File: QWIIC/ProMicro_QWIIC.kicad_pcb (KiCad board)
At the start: 2 copper layers, 17.8 x 30.5 mm, 19 parts, among them J1 Qwiic, J2 Qwiic, J3 Conn_01x02, J4 Conn_01x02, J5 Conn_01x03, J6 Conn_01x03, U1 ADS1015IDGS, U2 BME280

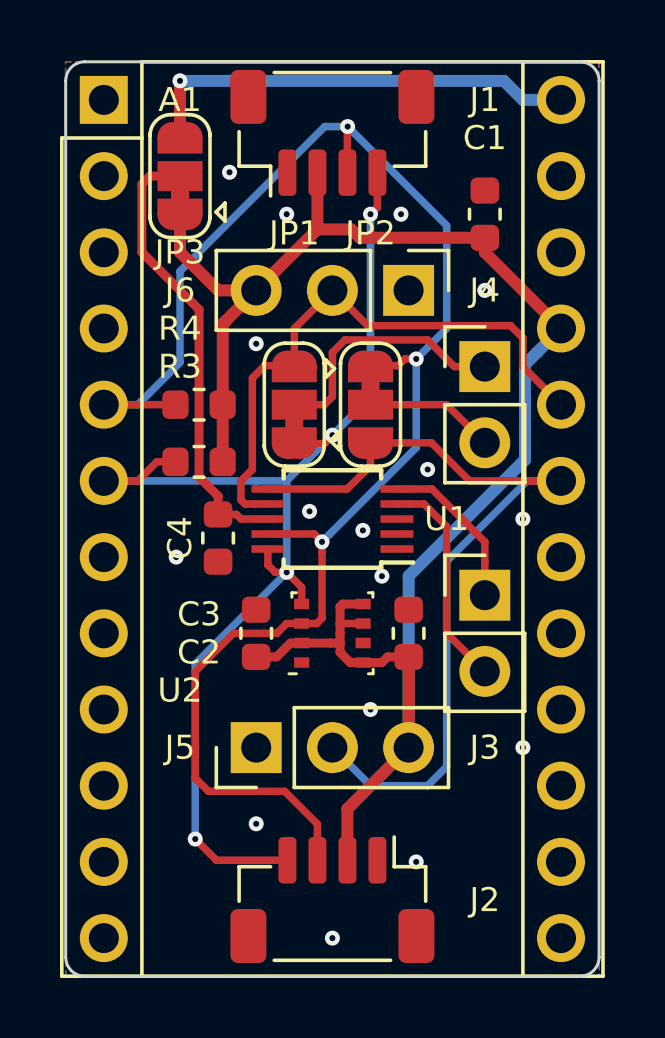
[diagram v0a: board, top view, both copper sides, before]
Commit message: make controller holes wide enough
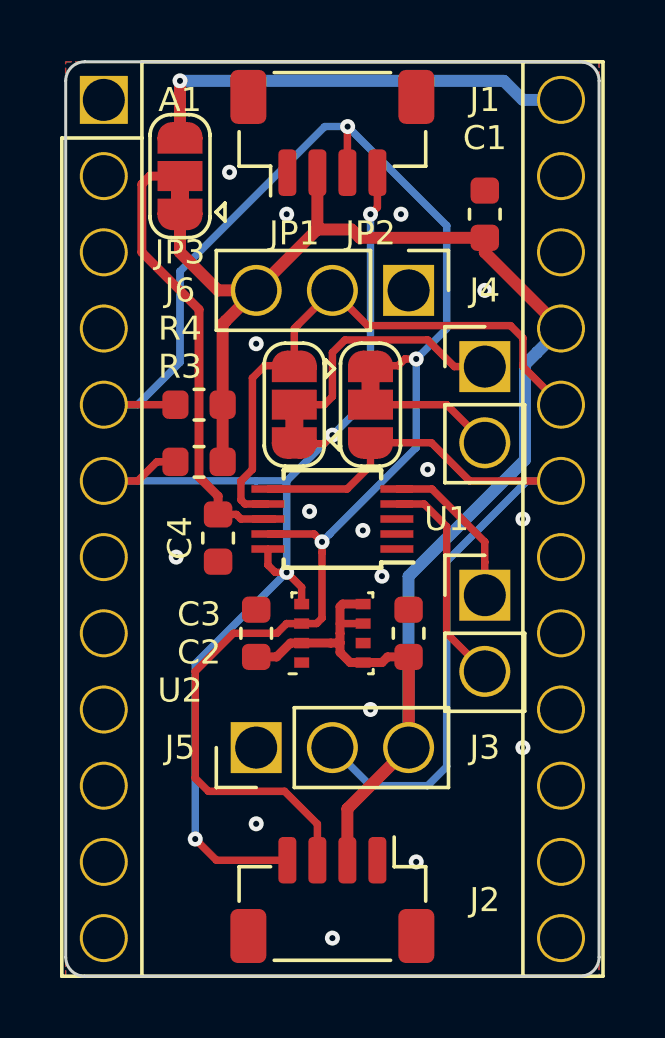
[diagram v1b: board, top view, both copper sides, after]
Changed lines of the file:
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@@
     (fp_line (start 1.27 -1.27) (end 1.27 6.35) (layer F.Fab) (width 0.1))
     (fp_line (start -0.635 -1.27) (end 1.27 -1.27) (layer F.Fab) (width 0.1))
-    (pad 3 thru_hole oval (at 0 5.08 270) (size 1.7 1.7) (drill 1) (layers *.Cu *.Mask)
-      (net 2 +3V3))
-    (pad 2 thru_hole oval (at 0 2.54 270) (size 1.7 1.7) (drill 1) (layers *.Cu *.Mask)
+    (pad 3 thru_hole circle (at 0 5.08 270) (size 1.7 1.7) (drill 1.4) (layers *.Cu *.Mask)
+      (net 2 +3V3))
+    (pad 2 thru_hole circle (at 0 2.54 270) (size 1.7 1.7) (drill 1.4) (layers *.Cu *.Mask)
       (net 8 A3))
-    (pad 1 thru_hole rect (at 0 0 270) (size 1.7 1.7) (drill 1) (layers *.Cu *.Mask)
+    (pad 1 thru_hole rect (at 0 0 270) (size 1.7 1.7) (drill 1.4) (layers *.Cu *.Mask)
       (net 1 GND))
     (model ${KISYS3DMOD}/Connector_PinHeader_2.54mm.3dshapes/PinHeader_1x03_P2.54mm_Vertical.wrl
@@
     (fp_line (start 1.27 -1.27) (end 1.27 6.35) (layer F.Fab) (width 0.1))
     (fp_line (start -0.635 -1.27) (end 1.27 -1.27) (layer F.Fab) (width 0.1))
-    (pad 3 thru_hole oval (at 0 5.08 90) (size 1.7 1.7) (drill 1) (layers *.Cu *.Mask)
-      (net 2 +3V3))
-    (pad 2 thru_hole oval (at 0 2.54 90) (size 1.7 1.7) (drill 1) (layers *.Cu *.Mask)
+    (pad 3 thru_hole circle (at 0 5.08 90) (size 1.7 1.7) (drill 1.4) (layers *.Cu *.Mask)
+      (net 2 +3V3))
+    (pad 2 thru_hole circle (at 0 2.54 90) (size 1.7 1.7) (drill 1.4) (layers *.Cu *.Mask)
       (net 9 A2))
-    (pad 1 thru_hole rect (at 0 0 90) (size 1.7 1.7) (drill 1) (layers *.Cu *.Mask)
+    (pad 1 thru_hole rect (at 0 0 90) (size 1.7 1.7) (drill 1.4) (layers *.Cu *.Mask)
       (net 1 GND))
     (model ${KISYS3DMOD}/Connector_PinHeader_2.54mm.3dshapes/PinHeader_1x03_P2.54mm_Vertical.wrl
@@
     (fp_line (start 1.27 -1.27) (end 1.27 3.81) (layer F.Fab) (width 0.1))
     (fp_line (start -0.635 -1.27) (end 1.27 -1.27) (layer F.Fab) (width 0.1))
-    (pad 2 thru_hole oval (at 0 2.54) (size 1.7 1.7) (drill 1) (layers *.Cu *.Mask)
+    (pad 2 thru_hole circle (at 0 2.54) (size 1.7 1.7) (drill 1.4) (layers *.Cu *.Mask)
       (net 6 "Net-(J4-Pad2)"))
-    (pad 1 thru_hole rect (at 0 0) (size 1.7 1.7) (drill 1) (layers *.Cu *.Mask)
+    (pad 1 thru_hole rect (at 0 0) (size 1.7 1.7) (drill 1.4) (layers *.Cu *.Mask)
       (net 7 "Net-(J4-Pad1)"))
     (model ${KISYS3DMOD}/Connector_PinHeader_2.54mm.3dshapes/PinHeader_1x02_P2.54mm_Vertical.wrl
@@
     (fp_line (start 1.27 -1.27) (end 1.27 3.81) (layer F.Fab) (width 0.1))
     (fp_line (start -0.635 -1.27) (end 1.27 -1.27) (layer F.Fab) (width 0.1))
-    (pad 2 thru_hole oval (at 0 2.54) (size 1.7 1.7) (drill 1) (layers *.Cu *.Mask)
+    (pad 2 thru_hole circle (at 0 2.54) (size 1.7 1.7) (drill 1.4) (layers *.Cu *.Mask)
       (net 10 /LIPO_VBAT))
-    (pad 1 thru_hole rect (at 0 0) (size 1.7 1.7) (drill 1) (layers *.Cu *.Mask)
+    (pad 1 thru_hole rect (at 0 0) (size 1.7 1.7) (drill 1.4) (layers *.Cu *.Mask)
       (net 5 "Net-(J3-Pad1)"))
     (model ${KISYS3DMOD}/Connector_PinHeader_2.54mm.3dshapes/PinHeader_1x02_P2.54mm_Vertical.wrl
@@
     (fp_line (start 16.8 29.3) (end 16.8 -1.5) (layer F.CrtYd) (width 0.05))
     (fp_line (start 16.8 29.3) (end -1.5 29.3) (layer F.CrtYd) (width 0.05))
-    (pad 24 thru_hole oval (at 15.24 0) (size 1.6 1.6) (drill 1) (layers *.Cu *.Mask)
+    (pad 24 thru_hole circle (at 15.24 0) (size 1.6 1.6) (drill 1.4) (layers *.Cu *.Mask)
       (net 11 +5V))
-    (pad 23 thru_hole oval (at 15.24 2.54) (size 1.6 1.6) (drill 1) (layers *.Cu *.Mask)
-      (net 1 GND))
-    (pad 22 thru_hole oval (at 15.24 5.08) (size 1.6 1.6) (drill 1) (layers *.Cu *.Mask))
-    (pad 12 thru_hole oval (at 0 27.94) (size 1.6 1.6) (drill 1) (layers *.Cu *.Mask))
-    (pad 21 thru_hole oval (at 15.24 7.62) (size 1.6 1.6) (drill 1) (layers *.Cu *.Mask)
-      (net 2 +3V3))
-    (pad 11 thru_hole oval (at 0 25.4) (size 1.6 1.6) (drill 1) (layers *.Cu *.Mask))
-    (pad 20 thru_hole oval (at 15.24 10.16) (size 1.6 1.6) (drill 1) (layers *.Cu *.Mask)
+    (pad 23 thru_hole circle (at 15.24 2.54) (size 1.6 1.6) (drill 1.4) (layers *.Cu *.Mask)
+      (net 1 GND))
+    (pad 22 thru_hole circle (at 15.24 5.08) (size 1.6 1.6) (drill 1.4) (layers *.Cu *.Mask))
+    (pad 12 thru_hole circle (at 0 27.94) (size 1.6 1.6) (drill 1.4) (layers *.Cu *.Mask))
+    (pad 21 thru_hole circle (at 15.24 7.62) (size 1.6 1.6) (drill 1.4) (layers *.Cu *.Mask)
+      (net 2 +3V3))
+    (pad 11 thru_hole circle (at 0 25.4) (size 1.6 1.6) (drill 1.4) (layers *.Cu *.Mask))
+    (pad 20 thru_hole circle (at 15.24 10.16) (size 1.6 1.6) (drill 1.4) (layers *.Cu *.Mask)
       (net 8 A3))
-    (pad 10 thru_hole oval (at 0 22.86) (size 1.6 1.6) (drill 1) (layers *.Cu *.Mask))
-    (pad 19 thru_hole oval (at 15.24 12.7) (size 1.6 1.6) (drill 1) (layers *.Cu *.Mask)
+    (pad 10 thru_hole circle (at 0 22.86) (size 1.6 1.6) (drill 1.4) (layers *.Cu *.Mask))
+    (pad 19 thru_hole circle (at 15.24 12.7) (size 1.6 1.6) (drill 1.4) (layers *.Cu *.Mask)
       (net 9 A2))
-    (pad 9 thru_hole oval (at 0 20.32) (size 1.6 1.6) (drill 1) (layers *.Cu *.Mask))
-    (pad 18 thru_hole oval (at 15.24 15.24) (size 1.6 1.6) (drill 1) (layers *.Cu *.Mask))
-    (pad 8 thru_hole oval (at 0 17.78) (size 1.6 1.6) (drill 1) (layers *.Cu *.Mask))
-    (pad 17 thru_hole oval (at 15.24 17.78) (size 1.6 1.6) (drill 1) (layers *.Cu *.Mask))
-    (pad 7 thru_hole oval (at 0 15.24) (size 1.6 1.6) (drill 1) (layers *.Cu *.Mask))
-    (pad 16 thru_hole oval (at 15.24 20.32) (size 1.6 1.6) (drill 1) (layers *.Cu *.Mask))
-    (pad 6 thru_hole oval (at 0 12.7) (size 1.6 1.6) (drill 1) (layers *.Cu *.Mask)
+    (pad 9 thru_hole circle (at 0 20.32) (size 1.6 1.6) (drill 1.4) (layers *.Cu *.Mask))
+    (pad 18 thru_hole circle (at 15.24 15.24) (size 1.6 1.6) (drill 1.4) (layers *.Cu *.Mask))
+    (pad 8 thru_hole circle (at 0 17.78) (size 1.6 1.6) (drill 1.4) (layers *.Cu *.Mask))
+    (pad 17 thru_hole circle (at 15.24 17.78) (size 1.6 1.6) (drill 1.4) (layers *.Cu *.Mask))
+    (pad 7 thru_hole circle (at 0 15.24) (size 1.6 1.6) (drill 1.4) (layers *.Cu *.Mask))
+    (pad 16 thru_hole circle (at 15.24 20.32) (size 1.6 1.6) (drill 1.4) (layers *.Cu *.Mask))
+    (pad 6 thru_hole circle (at 0 12.7) (size 1.6 1.6) (drill 1.4) (layers *.Cu *.Mask)
       (net 3 SCL))
-    (pad 15 thru_hole oval (at 15.24 22.86) (size 1.6 1.6) (drill 1) (layers *.Cu *.Mask))
-    (pad 5 thru_hole oval (at 0 10.16) (size 1.6 1.6) (drill 1) (layers *.Cu *.Mask)
+    (pad 15 thru_hole circle (at 15.24 22.86) (size 1.6 1.6) (drill 1.4) (layers *.Cu *.Mask))
+    (pad 5 thru_hole circle (at 0 10.16) (size 1.6 1.6) (drill 1.4) (layers *.Cu *.Mask)
       (net 4 SDA))
-    (pad 14 thru_hole oval (at 15.24 25.4) (size 1.6 1.6) (drill 1) (layers *.Cu *.Mask))
-    (pad 4 thru_hole oval (at 0 7.62) (size 1.6 1.6) (drill 1) (layers *.Cu *.Mask)
-      (net 1 GND))
-    (pad 13 thru_hole oval (at 15.24 27.94) (size 1.6 1.6) (drill 1) (layers *.Cu *.Mask))
-    (pad 3 thru_hole oval (at 0 5.08) (size 1.6 1.6) (drill 1) (layers *.Cu *.Mask))
-    (pad 2 thru_hole oval (at 0 2.54) (size 1.6 1.6) (drill 1) (layers *.Cu *.Mask))
-    (pad 1 thru_hole rect (at 0 0) (size 1.6 1.6) (drill 1) (layers *.Cu *.Mask))
+    (pad 14 thru_hole circle (at 15.24 25.4) (size 1.6 1.6) (drill 1.4) (layers *.Cu *.Mask))
+    (pad 4 thru_hole circle (at 0 7.62) (size 1.6 1.6) (drill 1.4) (layers *.Cu *.Mask)
+      (net 1 GND))
+    (pad 13 thru_hole circle (at 15.24 27.94) (size 1.6 1.6) (drill 1.4) (layers *.Cu *.Mask))
+    (pad 3 thru_hole circle (at 0 5.08) (size 1.6 1.6) (drill 1.4) (layers *.Cu *.Mask))
+    (pad 2 thru_hole circle (at 0 2.54) (size 1.6 1.6) (drill 1.4) (layers *.Cu *.Mask))
+    (pad 1 thru_hole rect (at 0 0) (size 1.6 1.6) (drill 1.4) (layers *.Cu *.Mask))
     (model ${KISYS3DMOD}/Module.3dshapes/Sparkfun_Pro_Micro.wrl
       (at (xyz 0 0 0))

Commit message: update PCBs to be stackable
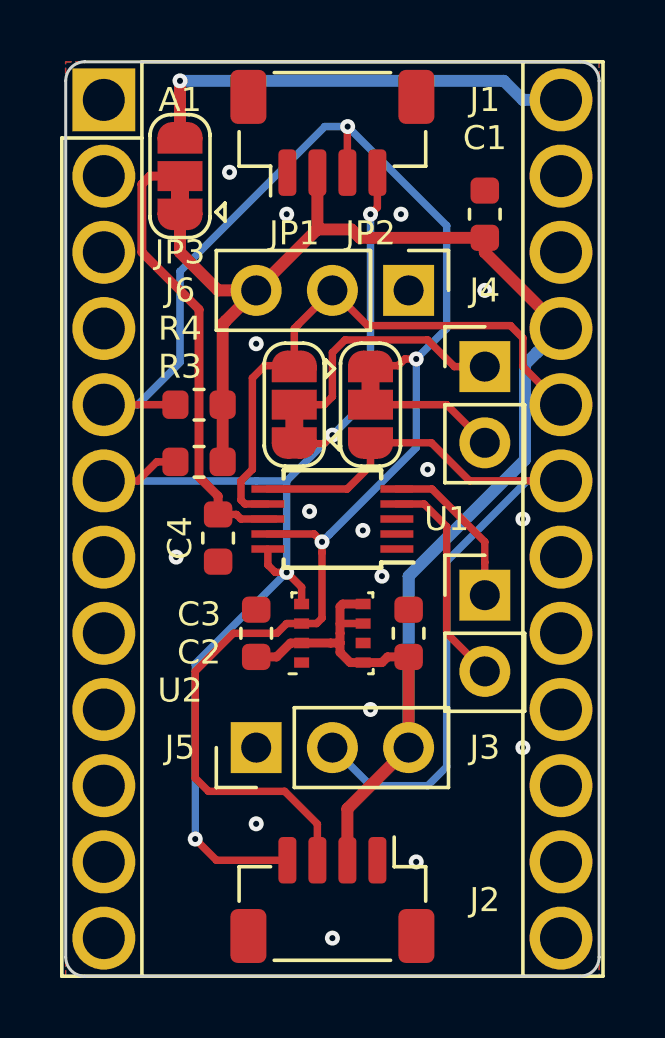
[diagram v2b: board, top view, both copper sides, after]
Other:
- board text added: "v1.1"
- board text removed: "v1.0"
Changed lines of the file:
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@@
   (title_block
     (title ProMicro_QWIIC)
-    (date 2020-06-01)
-    (rev v1.0)
+    (date 2020-11-21)
+    (rev v1.1)
   )
   (layers
@@
     (mod_text_size 1 1)
     (mod_text_width 0.15)
-    (pad_size 1.524 1.524)
-    (pad_drill 0.762)
+    (pad_size 2.1 2.1)
+    (pad_drill 1.4)
     (pad_to_mask_clearance 0)
     (aux_axis_origin 50.8 76.2)
@@
     (fp_line (start 1.27 -1.27) (end 1.27 6.35) (layer F.Fab) (width 0.1))
     (fp_line (start -0.635 -1.27) (end 1.27 -1.27) (layer F.Fab) (width 0.1))
-    (pad 3 thru_hole circle (at 0 5.08 270) (size 1.7 1.7) (drill 1.4) (layers *.Cu *.Mask)
-      (net 2 +3V3))
-    (pad 2 thru_hole circle (at 0 2.54 270) (size 1.7 1.7) (drill 1.4) (layers *.Cu *.Mask)
+    (pad 3 thru_hole circle (at 0 5.08 270) (size 1.7 1.7) (drill 1) (layers *.Cu *.Mask)
+      (net 2 +3V3))
+    (pad 2 thru_hole circle (at 0 2.54 270) (size 1.7 1.7) (drill 1) (layers *.Cu *.Mask)
       (net 8 A3))
-    (pad 1 thru_hole rect (at 0 0 270) (size 1.7 1.7) (drill 1.4) (layers *.Cu *.Mask)
+    (pad 1 thru_hole rect (at 0 0 270) (size 1.7 1.7) (drill 1) (layers *.Cu *.Mask)
       (net 1 GND))
     (model ${KISYS3DMOD}/Connector_PinHeader_2.54mm.3dshapes/PinHeader_1x03_P2.54mm_Vertical.wrl
@@
     (fp_line (start 1.27 -1.27) (end 1.27 6.35) (layer F.Fab) (width 0.1))
     (fp_line (start -0.635 -1.27) (end 1.27 -1.27) (layer F.Fab) (width 0.1))
-    (pad 3 thru_hole circle (at 0 5.08 90) (size 1.7 1.7) (drill 1.4) (layers *.Cu *.Mask)
-      (net 2 +3V3))
-    (pad 2 thru_hole circle (at 0 2.54 90) (size 1.7 1.7) (drill 1.4) (layers *.Cu *.Mask)
+    (pad 3 thru_hole circle (at 0 5.08 90) (size 1.7 1.7) (drill 1) (layers *.Cu *.Mask)
+      (net 2 +3V3))
+    (pad 2 thru_hole circle (at 0 2.54 90) (size 1.7 1.7) (drill 1) (layers *.Cu *.Mask)
       (net 9 A2))
-    (pad 1 thru_hole rect (at 0 0 90) (size 1.7 1.7) (drill 1.4) (layers *.Cu *.Mask)
+    (pad 1 thru_hole rect (at 0 0 90) (size 1.7 1.7) (drill 1) (layers *.Cu *.Mask)
       (net 1 GND))
     (model ${KISYS3DMOD}/Connector_PinHeader_2.54mm.3dshapes/PinHeader_1x03_P2.54mm_Vertical.wrl
@@
     (fp_line (start 1.27 -1.27) (end 1.27 3.81) (layer F.Fab) (width 0.1))
     (fp_line (start -0.635 -1.27) (end 1.27 -1.27) (layer F.Fab) (width 0.1))
-    (pad 2 thru_hole circle (at 0 2.54) (size 1.7 1.7) (drill 1.4) (layers *.Cu *.Mask)
+    (pad 2 thru_hole circle (at 0 2.54) (size 1.7 1.7) (drill 1) (layers *.Cu *.Mask)
       (net 6 "Net-(J4-Pad2)"))
-    (pad 1 thru_hole rect (at 0 0) (size 1.7 1.7) (drill 1.4) (layers *.Cu *.Mask)
+    (pad 1 thru_hole rect (at 0 0) (size 1.7 1.7) (drill 1) (layers *.Cu *.Mask)
       (net 7 "Net-(J4-Pad1)"))
     (model ${KISYS3DMOD}/Connector_PinHeader_2.54mm.3dshapes/PinHeader_1x02_P2.54mm_Vertical.wrl
@@
     (fp_line (start 1.27 -1.27) (end 1.27 3.81) (layer F.Fab) (width 0.1))
     (fp_line (start -0.635 -1.27) (end 1.27 -1.27) (layer F.Fab) (width 0.1))
-    (pad 2 thru_hole circle (at 0 2.54) (size 1.7 1.7) (drill 1.4) (layers *.Cu *.Mask)
+    (pad 2 thru_hole circle (at 0 2.54) (size 1.7 1.7) (drill 1) (layers *.Cu *.Mask)
       (net 10 /LIPO_VBAT))
-    (pad 1 thru_hole rect (at 0 0) (size 1.7 1.7) (drill 1.4) (layers *.Cu *.Mask)
+    (pad 1 thru_hole rect (at 0 0) (size 1.7 1.7) (drill 1) (layers *.Cu *.Mask)
       (net 5 "Net-(J3-Pad1)"))
     (model ${KISYS3DMOD}/Connector_PinHeader_2.54mm.3dshapes/PinHeader_1x02_P2.54mm_Vertical.wrl
@@
     (fp_line (start 16.8 29.3) (end 16.8 -1.5) (layer F.CrtYd) (width 0.05))
     (fp_line (start 16.8 29.3) (end -1.5 29.3) (layer F.CrtYd) (width 0.05))
-    (pad 24 thru_hole circle (at 15.24 0) (size 1.6 1.6) (drill 1.4) (layers *.Cu *.Mask)
+    (pad 24 thru_hole circle (at 15.24 0) (size 2.1 2.1) (drill 1.4) (layers *.Cu *.Mask)
       (net 11 +5V))
-    (pad 23 thru_hole circle (at 15.24 2.54) (size 1.6 1.6) (drill 1.4) (layers *.Cu *.Mask)
-      (net 1 GND))
-    (pad 22 thru_hole circle (at 15.24 5.08) (size 1.6 1.6) (drill 1.4) (layers *.Cu *.Mask))
-    (pad 12 thru_hole circle (at 0 27.94) (size 1.6 1.6) (drill 1.4) (layers *.Cu *.Mask))
-    (pad 21 thru_hole circle (at 15.24 7.62) (size 1.6 1.6) (drill 1.4) (layers *.Cu *.Mask)
-      (net 2 +3V3))
-    (pad 11 thru_hole circle (at 0 25.4) (size 1.6 1.6) (drill 1.4) (layers *.Cu *.Mask))
-    (pad 20 thru_hole circle (at 15.24 10.16) (size 1.6 1.6) (drill 1.4) (layers *.Cu *.Mask)
+    (pad 23 thru_hole circle (at 15.24 2.54) (size 2.1 2.1) (drill 1.4) (layers *.Cu *.Mask)
+      (net 1 GND))
+    (pad 22 thru_hole circle (at 15.24 5.08) (size 2.1 2.1) (drill 1.4) (layers *.Cu *.Mask))
+    (pad 12 thru_hole circle (at 0 27.94) (size 2.1 2.1) (drill 1.4) (layers *.Cu *.Mask))
+    (pad 21 thru_hole circle (at 15.24 7.62) (size 2.1 2.1) (drill 1.4) (layers *.Cu *.Mask)
+      (net 2 +3V3))
+    (pad 11 thru_hole circle (at 0 25.4) (size 2.1 2.1) (drill 1.4) (layers *.Cu *.Mask))
+    (pad 20 thru_hole circle (at 15.24 10.16) (size 2.1 2.1) (drill 1.4) (layers *.Cu *.Mask)
       (net 8 A3))
-    (pad 10 thru_hole circle (at 0 22.86) (size 1.6 1.6) (drill 1.4) (layers *.Cu *.Mask))
-    (pad 19 thru_hole circle (at 15.24 12.7) (size 1.6 1.6) (drill 1.4) (layers *.Cu *.Mask)
+    (pad 10 thru_hole circle (at 0 22.86) (size 2.1 2.1) (drill 1.4) (layers *.Cu *.Mask))
+    (pad 19 thru_hole circle (at 15.24 12.7) (size 2.1 2.1) (drill 1.4) (layers *.Cu *.Mask)
       (net 9 A2))
-    (pad 9 thru_hole circle (at 0 20.32) (size 1.6 1.6) (drill 1.4) (layers *.Cu *.Mask))
-    (pad 18 thru_hole circle (at 15.24 15.24) (size 1.6 1.6) (drill 1.4) (layers *.Cu *.Mask))
-    (pad 8 thru_hole circle (at 0 17.78) (size 1.6 1.6) (drill 1.4) (layers *.Cu *.Mask))
-    (pad 17 thru_hole circle (at 15.24 17.78) (size 1.6 1.6) (drill 1.4) (layers *.Cu *.Mask))
-    (pad 7 thru_hole circle (at 0 15.24) (size 1.6 1.6) (drill 1.4) (layers *.Cu *.Mask))
-    (pad 16 thru_hole circle (at 15.24 20.32) (size 1.6 1.6) (drill 1.4) (layers *.Cu *.Mask))
-    (pad 6 thru_hole circle (at 0 12.7) (size 1.6 1.6) (drill 1.4) (layers *.Cu *.Mask)
+    (pad 9 thru_hole circle (at 0 20.32) (size 2.1 2.1) (drill 1.4) (layers *.Cu *.Mask))
+    (pad 18 thru_hole circle (at 15.24 15.24) (size 2.1 2.1) (drill 1.4) (layers *.Cu *.Mask))
+    (pad 8 thru_hole circle (at 0 17.78) (size 2.1 2.1) (drill 1.4) (layers *.Cu *.Mask))
+    (pad 17 thru_hole circle (at 15.24 17.78) (size 2.1 2.1) (drill 1.4) (layers *.Cu *.Mask))
+    (pad 7 thru_hole circle (at 0 15.24) (size 2.1 2.1) (drill 1.4) (layers *.Cu *.Mask))
+    (pad 16 thru_hole circle (at 15.24 20.32) (size 2.1 2.1) (drill 1.4) (layers *.Cu *.Mask))
+    (pad 6 thru_hole circle (at 0 12.7) (size 2.1 2.1) (drill 1.4) (layers *.Cu *.Mask)
       (net 3 SCL))
-    (pad 15 thru_hole circle (at 15.24 22.86) (size 1.6 1.6) (drill 1.4) (layers *.Cu *.Mask))
-    (pad 5 thru_hole circle (at 0 10.16) (size 1.6 1.6) (drill 1.4) (layers *.Cu *.Mask)
+    (pad 15 thru_hole circle (at 15.24 22.86) (size 2.1 2.1) (drill 1.4) (layers *.Cu *.Mask))
+    (pad 5 thru_hole circle (at 0 10.16) (size 2.1 2.1) (drill 1.4) (layers *.Cu *.Mask)
       (net 4 SDA))
-    (pad 14 thru_hole circle (at 15.24 25.4) (size 1.6 1.6) (drill 1.4) (layers *.Cu *.Mask))
-    (pad 4 thru_hole circle (at 0 7.62) (size 1.6 1.6) (drill 1.4) (layers *.Cu *.Mask)
-      (net 1 GND))
-    (pad 13 thru_hole circle (at 15.24 27.94) (size 1.6 1.6) (drill 1.4) (layers *.Cu *.Mask))
-    (pad 3 thru_hole circle (at 0 5.08) (size 1.6 1.6) (drill 1.4) (layers *.Cu *.Mask))
-    (pad 2 thru_hole circle (at 0 2.54) (size 1.6 1.6) (drill 1.4) (layers *.Cu *.Mask))
-    (pad 1 thru_hole rect (at 0 0) (size 1.6 1.6) (drill 1.4) (layers *.Cu *.Mask))
+    (pad 14 thru_hole circle (at 15.24 25.4) (size 2.1 2.1) (drill 1.4) (layers *.Cu *.Mask))
+    (pad 4 thru_hole circle (at 0 7.62) (size 2.1 2.1) (drill 1.4) (layers *.Cu *.Mask)
+      (net 1 GND))
+    (pad 13 thru_hole circle (at 15.24 27.94) (size 2.1 2.1) (drill 1.4) (layers *.Cu *.Mask))
+    (pad 3 thru_hole circle (at 0 5.08) (size 2.1 2.1) (drill 1.4) (layers *.Cu *.Mask))
+    (pad 2 thru_hole circle (at 0 2.54) (size 2.1 2.1) (drill 1.4) (layers *.Cu *.Mask))
+    (pad 1 thru_hole rect (at 0 0) (size 2.1 2.1) (drill 1.4) (layers *.Cu *.Mask))
     (model ${KISYS3DMOD}/Module.3dshapes/Sparkfun_Pro_Micro.wrl
       (at (xyz 0 0 0))
@@
     (arrow2b (pts (xy 49.53 72.39) (xy 50.656504 71.803579)))
   )
-  (gr_text v1.0 (at 58.42 93.98) (layer B.SilkS)
+  (gr_text v1.1 (at 58.42 93.98) (layer B.SilkS)
     (effects (font (size 0.9 0.9) (thickness 0.2)) (justify mirror))
   )

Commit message: update design
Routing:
- net +3V3: track 57.3 -> 59.5 mm
- net SDA: track 55.1 -> 54.2 mm
- net GND: vias 16 -> 19
